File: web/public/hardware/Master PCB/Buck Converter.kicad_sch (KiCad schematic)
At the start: 8 parts, among them U2 TLV62568DBV

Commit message: Add EEPROM
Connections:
- net 3V3 renamed +3V3
- net 5V renamed +5V
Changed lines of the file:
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@@
+    (stroke (width 0) (type default))
+  )
+  (wire (pts (xy 99.06 83.82) (xy 99.06 86.36))
     (stroke (width 0) (type default))
   )
@@
   )
   (wire (pts (xy 139.7 88.9) (xy 142.24 88.9))
+    (stroke (width 0) (type default))
+  )
+  (wire (pts (xy 176.53 83.82) (xy 176.53 86.36))
     (stroke (width 0) (type default))
   )
@@
   (text "Buck converter for STM32" (at 91.44 74.93 0)
     (effects (font (size 1.27 1.27)) (justify left bottom))
-  )
-  (hierarchical_label "5V" (shape input) (at 99.06 86.36 180) (fields_autoplaced)
-    (effects (font (size 1.27 1.27)) (justify right))
-  )
-  (hierarchical_label "3V3" (shape input) (at 176.53 86.36 0) (fields_autoplaced)
-    (effects (font (size 1.27 1.27)) (justify left))
   )
   (symbol (lib_id "power:GND") (at 132.08 96.52 0) (unit 1)
@@
         )
       )
+    )
+  )
+  (symbol (lib_id "power:+3V3") (at 176.53 83.82 0) (unit 1)
+    (in_bom yes) (on_board yes) (dnp no)
+    (property "Reference" "#PWR042" (at 176.53 87.63 0)
+      (effects (font (size 1.27 1.27)) hide)
+    )
+    (property "Value" "+3V3" (at 176.53 80.01 0)
+      (effects (font (size 1.27 1.27)))
+    )
+    (property "Footprint" "" (at 176.53 83.82 0)
+      (effects (font (size 1.27 1.27)) hide)
+    )
+    (property "Datasheet" "" (at 176.53 83.82 0)
+      (effects (font (size 1.27 1.27)) hide)
+    )
+    (pin "1")
+    (instances
+      (project "Master PCB"
+        (path "/61606422-4f73-4717-9ce6-6ac5e634e7ae/a1a1ce69-c437-4004-bd49-cc56d8ed4149"
+          (reference "#PWR042") (unit 1)
+        )
+      )
+    )
+  )
+  (symbol (lib_id "power:+5V") (at 99.06 83.82 0) (unit 1)
+    (in_bom yes) (on_board yes) (dnp no)
+    (property "Reference" "#PWR041" (at 99.06 87.63 0)
+      (effects (font (size 1.27 1.27)) hide)
+    )
+    (property "Value" "+5V" (at 99.06 80.01 0)
+      (effects (font (size 1.27 1.27)))
+    )
+    (property "Footprint" "" (at 99.06 83.82 0)
+      (effects (font (size 1.27 1.27)) hide)
+    )
+    (property "Datasheet" "" (at 99.06 83.82 0)
+      (effects (font (size 1.27 1.27)) hide)
+    )
+    (pin "1")
+    (instances
+      (project "Master PCB"
+        (path "/61606422-4f73-4717-9ce6-6ac5e634e7ae/a1a1ce69-c437-4004-bd49-cc56d8ed4149"
+          (reference "#PWR041") (unit 1)
+        )
+      )

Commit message: Finish schematic and start routing PCB
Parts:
- C13, C14, C15: footprint (none) -> Capacitor_SMD:C_0805_2012Metric_Pad1.18x1.45mm_HandSolder
- L1: footprint (none) -> Inductor_SMD:L_0805_2012Metric_Pad1.15x1.40mm_HandSolder
- R3: footprint (none) -> Resistor_SMD:R_0805_2012Metric_Pad1.20x1.40mm_HandSolder
- R4: value 200K -> 680K; footprint (none) -> Resistor_SMD:R_0805_2012Metric_Pad1.20x1.40mm_HandSolder
- R5: value 100K -> 150K; footprint (none) -> Resistor_SMD:R_0805_2012Metric_Pad1.20x1.40mm_HandSolder
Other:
- note added: "Vout = 0.6V * (1 + R4/R5)"
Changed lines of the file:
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@@
     (stroke (width 0) (type default))
+  )
+  (text "Vout = 0.6V * (1 + R4/R5)" (at 147.32 113.03 0)
+    (effects (font (size 1.27 1.27)) (justify left bottom))
   )
   (text "Buck converter for STM32" (at 91.44 74.93 0)
     (effects (font (size 1.27 1.27)) (justify left bottom))
   )
+  (label "Vout" (at 167.64 86.36 180) (fields_autoplaced)
+    (effects (font (size 1.27 1.27)) (justify right bottom))
+  )
   (symbol (lib_id "power:GND") (at 132.08 96.52 0) (unit 1)
     (in_bom yes) (on_board yes) (dnp no) (fields_autoplaced)
@@
   (symbol (lib_id "Device:R_Small_US") (at 160.02 97.79 0) (unit 1)
     (in_bom yes) (on_board yes) (dnp no) (fields_autoplaced)
-    (property "Reference" "R4" (at 162.56 96.52 0)
-      (effects (font (size 1.27 1.27)) (justify left))
-    )
-    (property "Value" "200K" (at 162.56 99.06 0)
-      (effects (font (size 1.27 1.27)) (justify left))
-    )
-    (property "Footprint" "" (at 160.02 97.79 0)
+    (property "Reference" "R4" (at 162.56 97.155 0)
+      (effects (font (size 1.27 1.27)) (justify left))
+    )
+    (property "Value" "680K" (at 162.56 99.695 0)
+      (effects (font (size 1.27 1.27)) (justify left))
+    )
+    (property "Footprint" "Resistor_SMD:R_0805_2012Metric_Pad1.20x1.40mm_HandSolder" (at 160.02 97.79 0)
       (effects (font (size 1.27 1.27)) hide)
     )
@@
   (symbol (lib_id "Device:R_Small_US") (at 160.02 105.41 0) (unit 1)
     (in_bom yes) (on_board yes) (dnp no) (fields_autoplaced)
-    (property "Reference" "R5" (at 162.56 104.14 0)
-      (effects (font (size 1.27 1.27)) (justify left))
-    )
-    (property "Value" "100K" (at 162.56 106.68 0)
-      (effects (font (size 1.27 1.27)) (justify left))
-    )
-    (property "Footprint" "" (at 160.02 105.41 0)
+    (property "Reference" "R5" (at 162.56 104.775 0)
+      (effects (font (size 1.27 1.27)) (justify left))
+    )
+    (property "Value" "150K" (at 162.56 107.315 0)
+      (effects (font (size 1.27 1.27)) (justify left))
+    )
+    (property "Footprint" "Resistor_SMD:R_0805_2012Metric_Pad1.20x1.40mm_HandSolder" (at 160.02 105.41 0)
       (effects (font (size 1.27 1.27)) hide)
     )
@@
       (effects (font (size 1.27 1.27)) (justify left))
     )
-    (property "Footprint" "" (at 171.45 91.44 0)
+    (property "Footprint" "Capacitor_SMD:C_0805_2012Metric_Pad1.18x1.45mm_HandSolder" (at 171.45 91.44 0)
       (effects (font (size 1.27 1.27)) hide)
     )
@@
       (effects (font (size 1.27 1.27)) (justify left))
     )
-    (property "Footprint" "" (at 113.03 88.9 0)
+    (property "Footprint" "Capacitor_SMD:C_0805_2012Metric_Pad1.18x1.45mm_HandSolder" (at 113.03 88.9 0)
       (effects (font (size 1.27 1.27)) hide)
     )
@@
       (effects (font (size 1.27 1.27)))
     )
-    (property "Footprint" "" (at 144.78 86.36 0)
+    (property "Footprint" "Inductor_SMD:L_0805_2012Metric_Pad1.15x1.40mm_HandSolder" (at 144.78 86.36 0)
       (effects (font (size 1.27 1.27)) hide)
     )
@@
       (effects (font (size 1.27 1.27)) (justify left))
     )
-    (property "Footprint" "" (at 104.14 88.9 0)
+    (property "Footprint" "Resistor_SMD:R_0805_2012Metric_Pad1.20x1.40mm_HandSolder" (at 104.14 88.9 0)
       (effects (font (size 1.27 1.27)) hide)
     )
@@
       (effects (font (size 1.27 1.27)) (justify left))
     )
-    (property "Footprint" "" (at 149.86 91.44 0)
-      (effects (font (size 1.27 1.27)) hide)
-    )
+    (property "Footprint" "Capacitor_SMD:C_0805_2012Metric_Pad1.18x1.45mm_HandSolder" (at 149.86 91.44 0)
+      (effects (font (size 1.27 1.27)) hide)
+    )

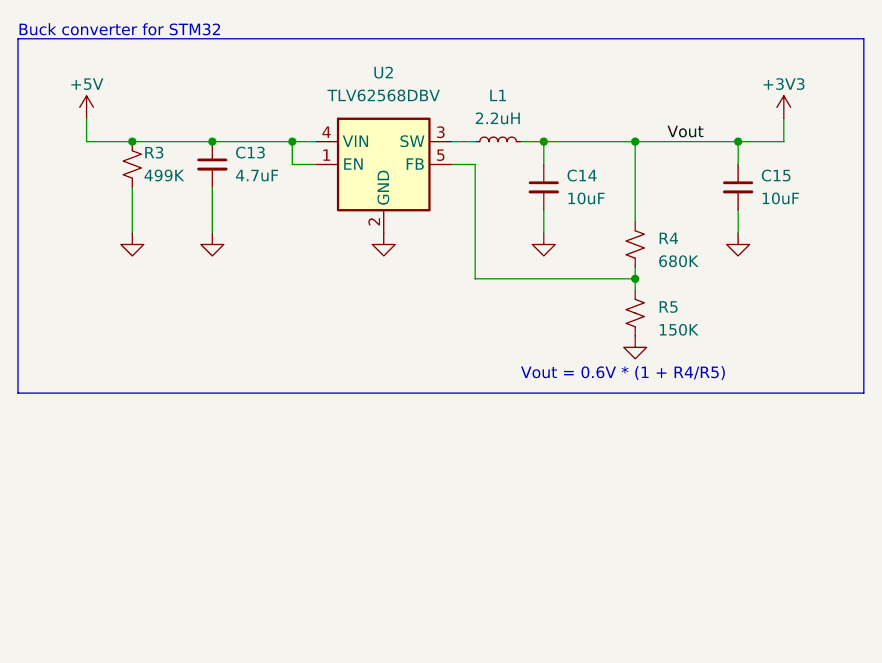
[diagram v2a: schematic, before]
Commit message: Add labels, replace inductor, update routing
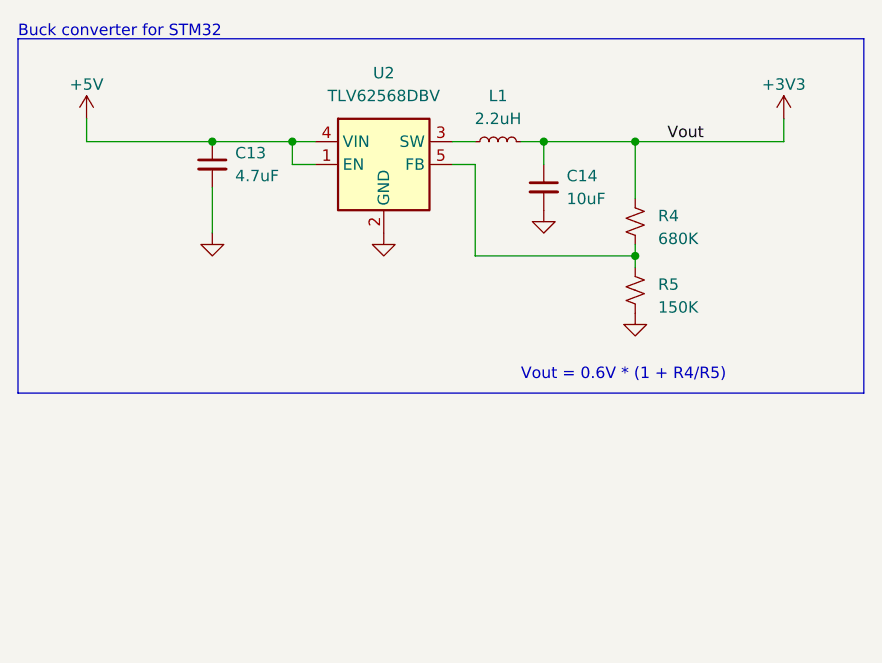
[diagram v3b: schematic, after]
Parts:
- removed C15: 10uF, Capacitor_SMD:C_0805_2012Metric_Pad1.18x1.45mm_HandSolder, symbol Device:C_Small
- removed R3: 499K, Resistor_SMD:R_0805_2012Metric_Pad1.20x1.40mm_HandSolder, symbol Device:R_Small_US
- L1: footprint Inductor_SMD:L_0805_2012Metric_Pad1.15x1.40mm_HandSolder -> Inductor_SMD_Other:L_4.0x4.0_H1.8
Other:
- moved on the sheet: R4, R5

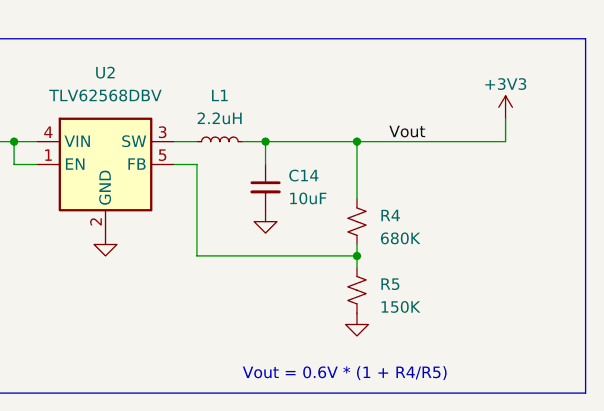
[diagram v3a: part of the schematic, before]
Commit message: Update buck converter resistor values
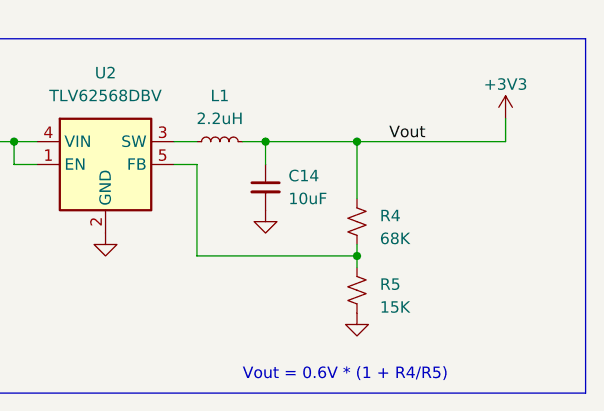
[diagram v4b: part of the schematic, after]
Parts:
- R4: value 680K -> 68K
- R5: value 150K -> 15K
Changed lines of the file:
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@@
       (effects (font (size 1.27 1.27)) (justify left))
     )
-    (property "Value" "680K" (at 162.56 97.155 0)
+    (property "Value" "68K" (at 162.56 97.155 0)
       (effects (font (size 1.27 1.27)) (justify left))
     )
@@
       (effects (font (size 1.27 1.27)) (justify left))
     )
-    (property "Value" "150K" (at 162.56 104.775 0)
+    (property "Value" "15K" (at 162.56 104.775 0)
       (effects (font (size 1.27 1.27)) (justify left))
     )

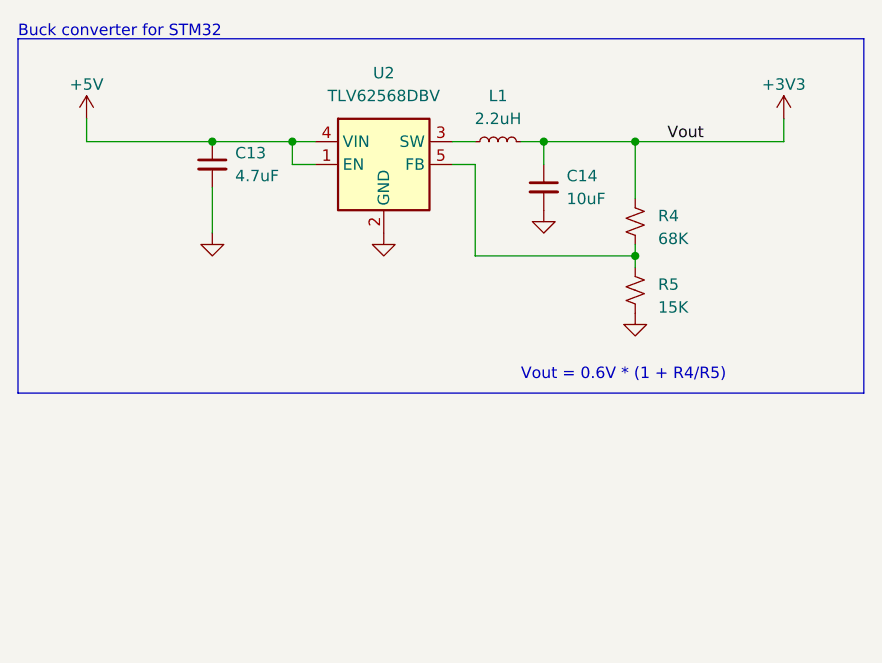
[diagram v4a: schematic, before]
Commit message: Move power indicator LEDs to buck converter schematic
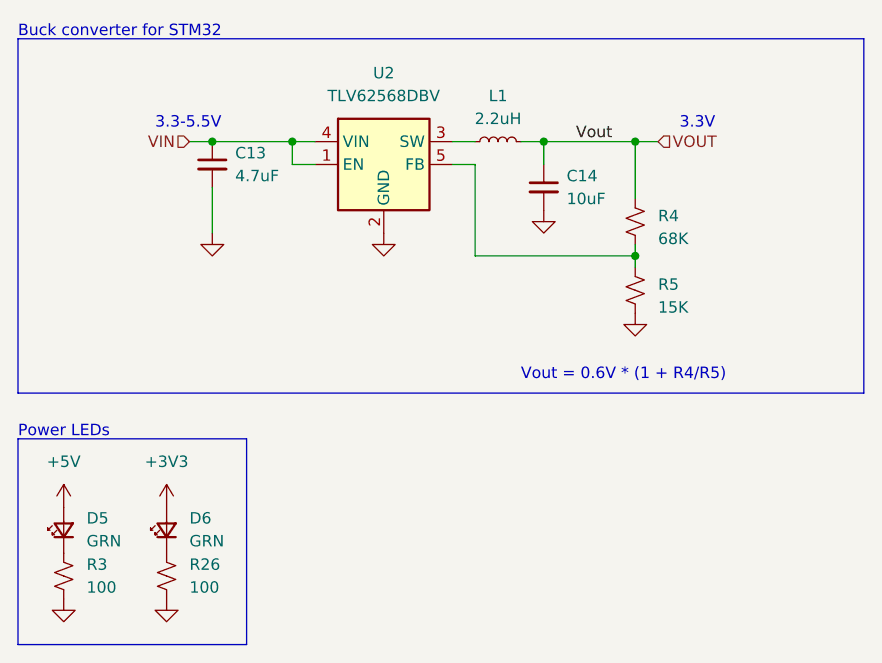
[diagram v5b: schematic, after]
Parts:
- added D5, D6: GRN, LED_SMD:LED_0805_2012Metric_Pad1.15x1.40mm_HandSolder, symbol Device:LED_Small
- added R26, R3: 100, Resistor_SMD:R_0805_2012Metric_Pad1.20x1.40mm_HandSolder, symbol Device:R_Small_US
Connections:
- net +3V3: now also D6.2 (A); no longer C14.1, L1.2, R4.1
- net +5V: now also D5.2 (A); no longer C13.1, U2.1 (EN), U2.4 (VIN)
- net GND: now also R26.2, R3.2
- new net: D6.1 (K), R26.1
- new net: D5.1 (K), R3.1
- new net VIN: C13.1, U2.1 (EN), U2.4 (VIN)
- new net VOUT: C14.1, L1.2, R4.1
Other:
- note added: "3.3-5.5V"
- note added: "3.3V"
- note added: "Power LEDs"

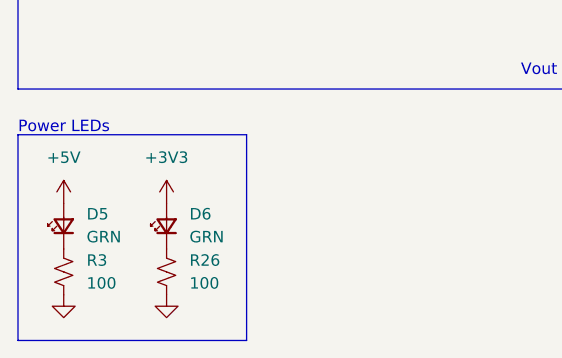
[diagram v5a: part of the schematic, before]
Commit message: Update indicator LED resistor values
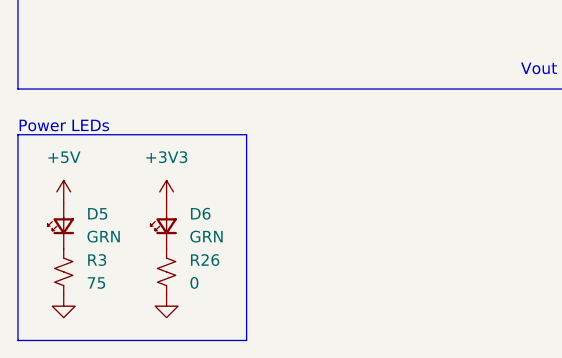
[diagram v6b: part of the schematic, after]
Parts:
- R26: value 100 -> 0
- R3: value 100 -> 75
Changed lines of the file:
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@@
       (effects (font (size 1.27 1.27)) (justify left))
     )
-    (property "Value" "100" (at 99.06 135.89 0)
+    (property "Value" "75" (at 99.06 135.89 0)
       (effects (font (size 1.27 1.27)) (justify left))
     )
@@
       (effects (font (size 1.27 1.27)) (justify left))
     )
-    (property "Value" "100" (at 110.49 135.89 0)
+    (property "Value" "0" (at 110.49 135.89 0)
       (effects (font (size 1.27 1.27)) (justify left))
     )

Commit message: Change LED resistor values
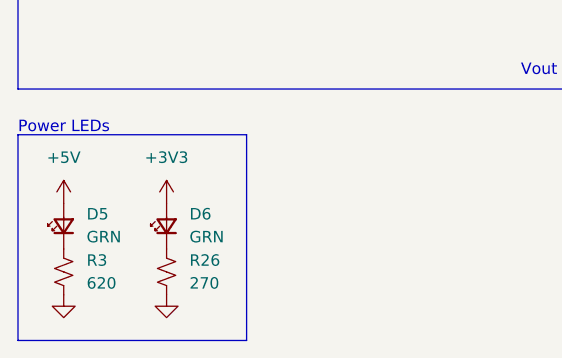
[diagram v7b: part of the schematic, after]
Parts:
- R26: value 0 -> 270
- R3: value 75 -> 620
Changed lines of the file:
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@@
       (effects (font (size 1.27 1.27)) (justify left))
     )
-    (property "Value" "75" (at 99.06 135.89 0)
+    (property "Value" "620" (at 99.06 135.89 0)
       (effects (font (size 1.27 1.27)) (justify left))
     )
@@
       (effects (font (size 1.27 1.27)) (justify left))
     )
-    (property "Value" "0" (at 110.49 135.89 0)
+    (property "Value" "270" (at 110.49 135.89 0)
       (effects (font (size 1.27 1.27)) (justify left))
     )
